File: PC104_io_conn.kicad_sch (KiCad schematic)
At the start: 1 part, among them P14 Conn_04x26_Pin

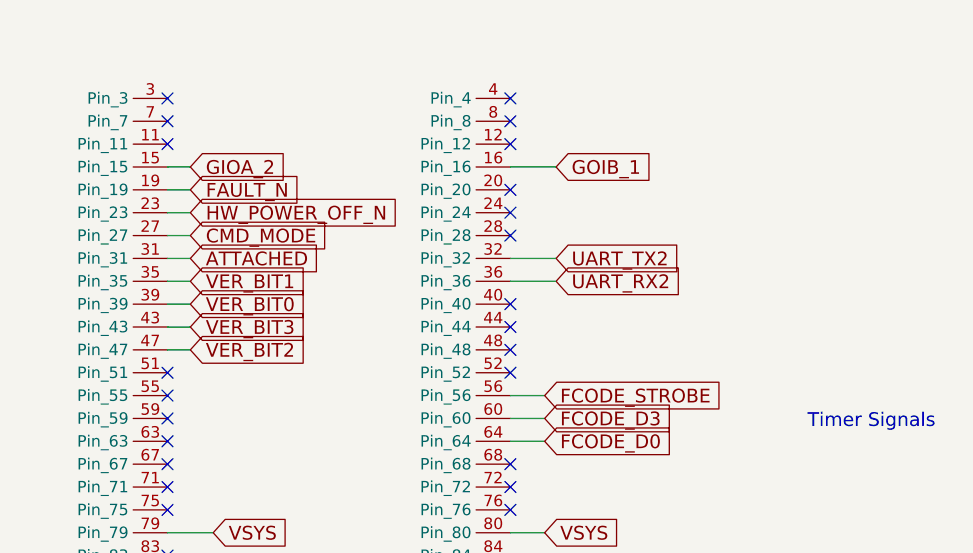
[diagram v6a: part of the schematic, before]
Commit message: Add active/standby configuration for the board
Signed-off-by: Corey Minyard <corey@minyard.net>
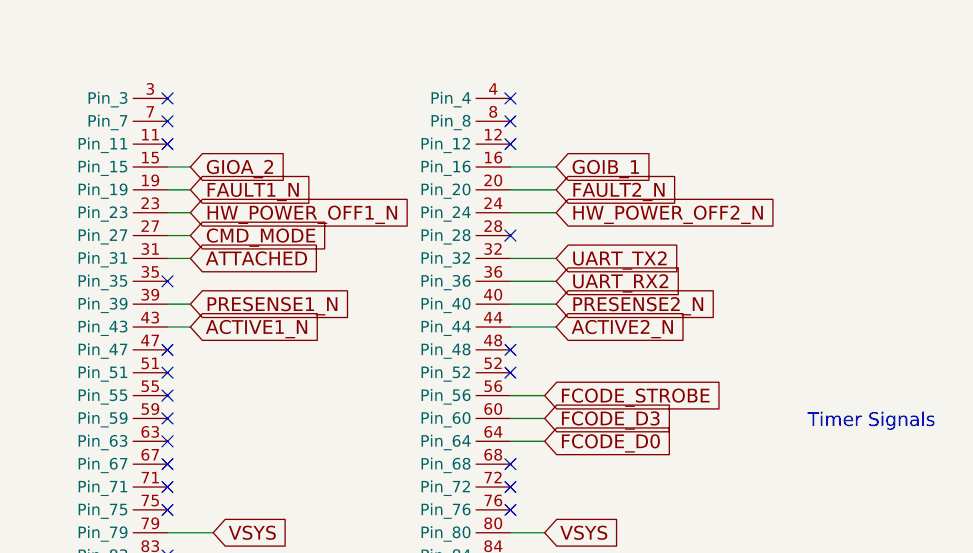
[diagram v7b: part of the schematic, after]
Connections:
- net FAULT2_N: now reaches P14.20 (Pin_20)
- net HW_POWER_OFF2_N: now reaches P14.24 (Pin_24)
- net PRESENSE2_N: now reaches P14.40 (Pin_40)
- net ACTIVE2_N: now reaches P14.44 (Pin_44)
- net FAULT_N renamed FAULT1_N
- net HW_POWER_OFF_N renamed HW_POWER_OFF1_N
- net VER_BIT0 renamed PRESENSE1_N
- net VER_BIT1: no longer names the net of P14.35 (Pin_35)
- net VER_BIT2: no longer names the net of P14.47 (Pin_47)
- net VER_BIT3 renamed ACTIVE1_N
- no-connect marks 71 -> 69

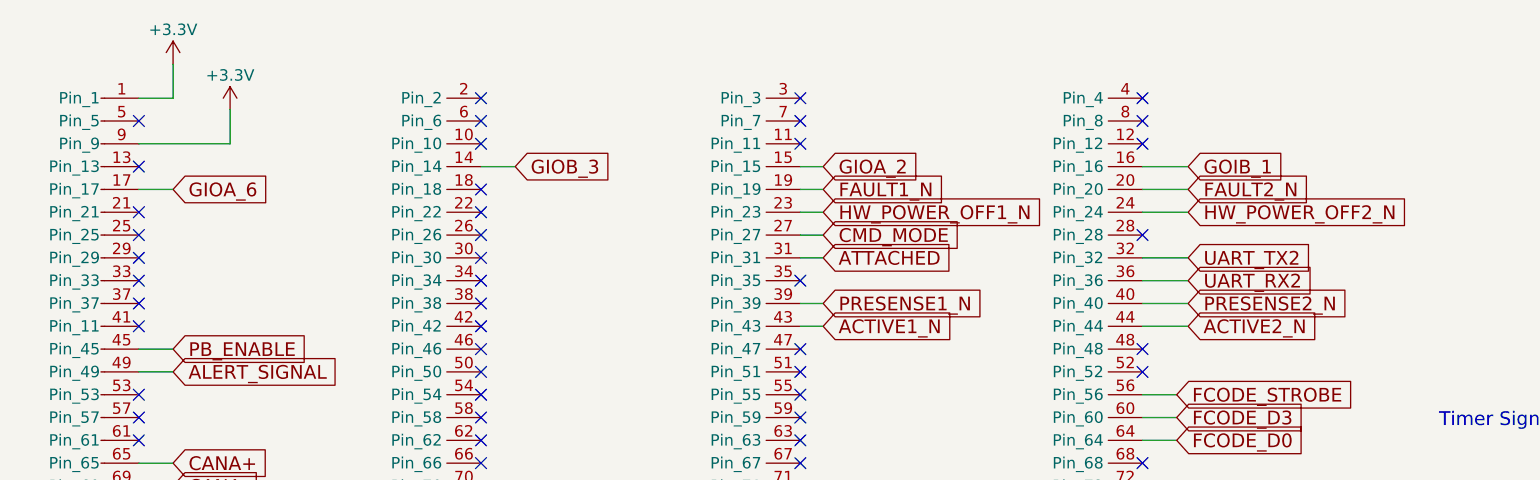
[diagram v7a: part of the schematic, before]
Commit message: Start working on active/standby handling
Signed-off-by: Corey Minyard <corey@minyard.net>
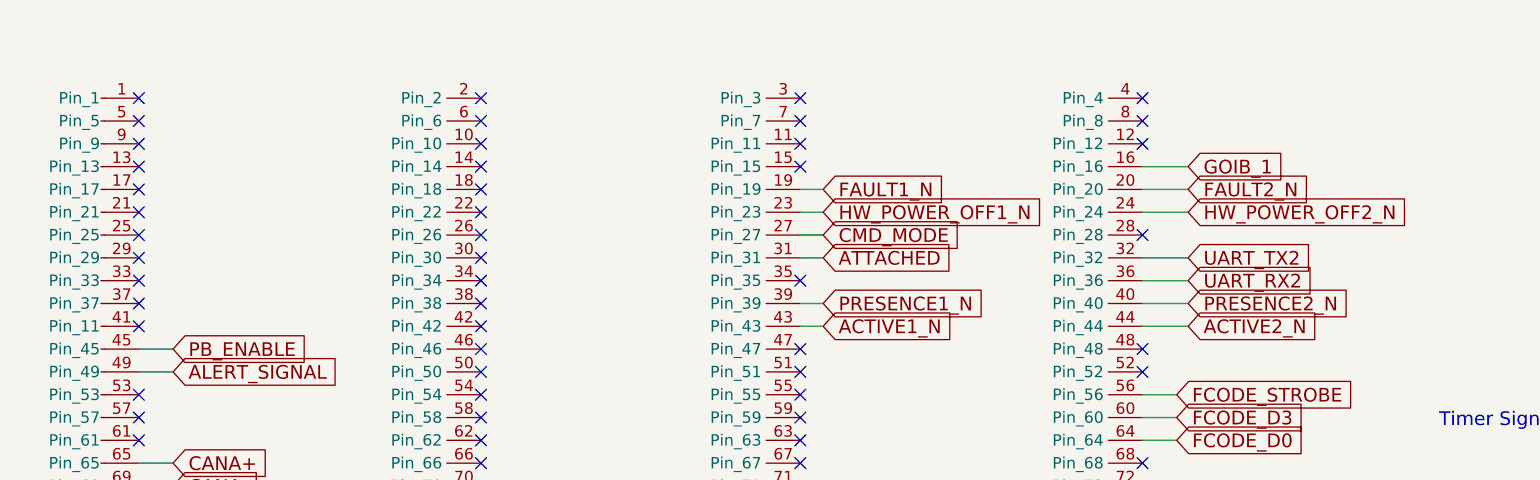
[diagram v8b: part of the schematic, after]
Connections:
- net +3.3V: no longer names the net of P14.1 (Pin_1)
- net +3.3V: no longer P14.9 (Pin_9)
- net GIOA_2: no longer names the net of P14.15 (Pin_15)
- net GIOA_6: no longer names the net of P14.17 (Pin_17)
- net GIOB_3: no longer names the net of P14.14 (Pin_14)
- net PRESENSE1_N renamed PRESENCE1_N
- net PRESENSE2_N renamed PRESENCE2_N
- no-connect marks 69 -> 74
